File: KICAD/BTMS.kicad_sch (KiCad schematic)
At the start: 218 parts, among them J1 Batt_Ballance, J10 PWR_SW, J2 USB_C_Receptacle_4085, J3 AUX_Charge, J4 Battery_IO, J5 Power_Out, J6 DSKY, J7 BatteryPTC, J8 Heater, J9 ICSP, Q1 DMN65D8L, Q2 SSM3K341R, Q3 BSS84-7-F, Q5 DMN65D8L, Q6 SSM3K341R, Q7 BSS84-7-F, SW1 PTS526, U1 FAN3100TSX, U10 ACS711xLCTR-25AB, U11 ISL95808HRZ, U12 AON7522E, U13 AON7522E, U14 FAN3100TSX, U15 AON7522E, U16 LM62CIM3/NOPB, U17 FAN3100TSX, U18 AP62250Z6, U19 AP62250Z6, U2 DMP2240UDM, U20 dsPIC30F4011-PT, U21 FT230XQ, U22 MIC5504-3.3YM5, U23 DMP2240UDM, U24 DMP2240UDM, U25 DMP2240UDM, U26 DMP2240UDM, U3 Q294700DSGR, U4 ACS711xLCTR-25AB, U5 IS281-4, U6 SCF4030-12-0X, U7 AP33772, U8 IS281-4, U9 AONR21321

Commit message: Updated schematic and board to reflect changes made on prototype.
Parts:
- removed D10, D11: D_Schottky40V, Diode_SMD:D_0603_1608Metric, symbol Device:D
- removed R19: 0R, Resistor_SMD:R_1206_3216Metric, symbol Device:R
- added C64, C65: 10uf 25v BF, Capacitor_SMD:C_0805_2012Metric, symbol Device:C
- JP1: value SolderJumper_2_Open -> SolderJumper
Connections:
- net GND: now also C64.2, C65.2
- net VBUS: now also R17.1, U7.24 (VCC), C64.1, C65.1
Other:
- note added: "Battery Current and Output Control"
- note added: "Boost Drive"
- note added: "Buck Drive"
- note added: "Buck-Boost converter system"
- note added: "Cell Ballancing Control"
- note added: "Cell Voltage Analog Input Control"
- note added: "Charge Input Handling."
- note added: "Hardware Over Volt Protection"
- note added: "Heater Control"
- note added: "Power Enable Handling"
- note added: "USB serial"
- note added: "dsPIC and analog filtering."
- note removed: "Remove this 0 ohm resistor if USB charging is not desired."
- moved on the sheet: C1, C11, C12, C14, C15, C17, C19, C2, C21, C23, C25, C27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

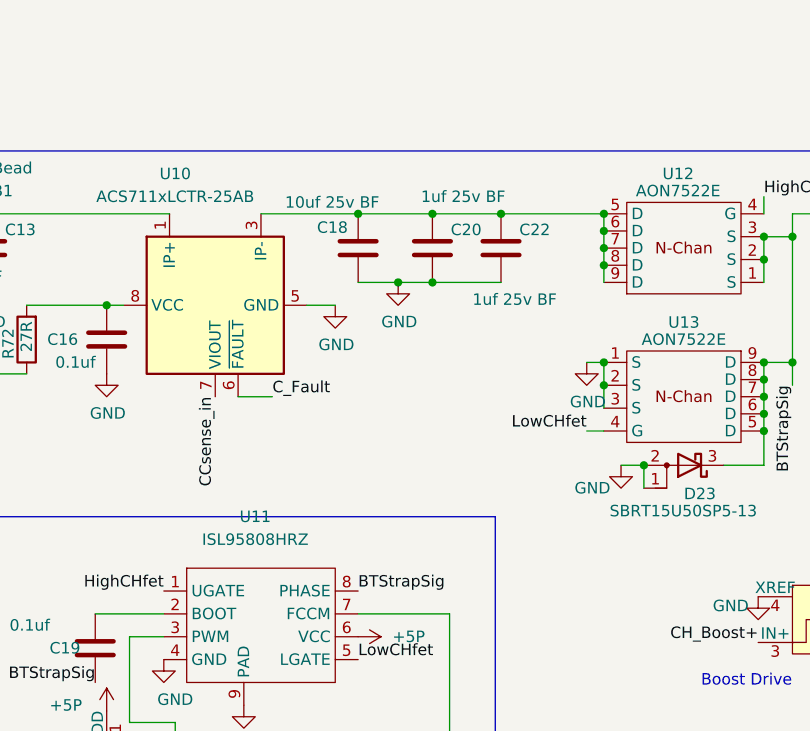
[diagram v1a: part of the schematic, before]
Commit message: Cleaned up some things in schematic and board. Deleted files not needed that were added to repo by mistake. Added 30uF of capacitors to input side of buck-boost converter.
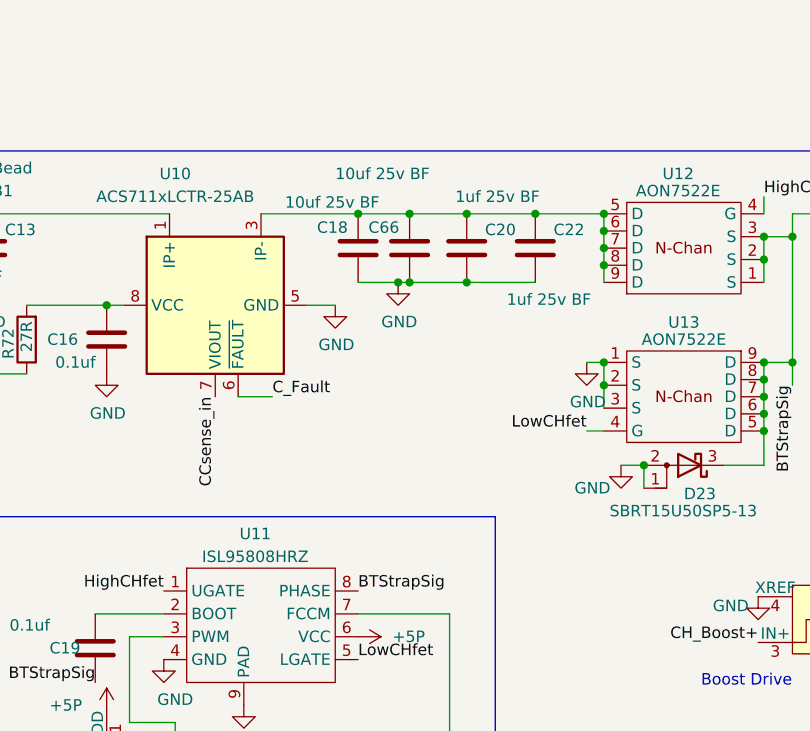
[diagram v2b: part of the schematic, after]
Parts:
- added C66: 10uf 25v BF, Capacitor_SMD:C_0805_2012Metric, symbol Device:C
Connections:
- net GND: now also C66.2
- net at C18.1, C20.1, C22.1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: now also C66.1
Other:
- moved on the sheet: C20, C22
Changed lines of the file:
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@@
   (junction (at 128.27 151.13) (diameter 0) (color 0 0 0 0)
   )
-  (junction (at 267.335 41.91) (diameter 0) (color 0 0 0 0)
+  (junction (at 264.795 41.91) (diameter 0) (color 0 0 0 0)
   )
   (junction (at 322.58 73.66) (diameter 0) (color 0 0 0 0)
@@
   (junction (at 126.365 292.1) (diameter 0) (color 0 0 0 0)
   )
+  (junction (at 278.765 41.91) (diameter 0) (color 0 0 0 0)
+  )
   (junction (at 219.075 395.605) (diameter 0) (color 0 0 0 0)
   )
@@
   (junction (at 348.615 51.435) (diameter 0) (color 0 0 0 0)
   )
-  (junction (at 274.955 41.91) (diameter 0) (color 0 0 0 0)
-  )
   (junction (at 538.48 151.13) (diameter 0) (color 0 0 0 0)
   )
@@
   (junction (at 424.18 81.915) (diameter 0) (color 0 0 0 0)
   )
+  (junction (at 271.145 41.91) (diameter 0) (color 0 0 0 0)
+  )
   (junction (at 523.24 46.99) (diameter 0) (color 0 0 0 0)
   )
@@
   (junction (at 537.845 327.025) (diameter 0) (color 0 0 0 0)
   )
+  (junction (at 264.795 49.53) (diameter 0) (color 0 0 0 0)
+  )
   (junction (at 535.305 327.025) (diameter 0) (color 0 0 0 0)
   )
@@
   (junction (at 245.745 276.86) (diameter 0) (color 0 0 0 0)
   )
-  (junction (at 267.335 49.53) (diameter 0) (color 0 0 0 0)
-  )
   (junction (at 245.745 269.24) (diameter 0) (color 0 0 0 0)
   )
@@
   (junction (at 464.82 260.985) (diameter 0) (color 0 0 0 0)
   )
+  (junction (at 271.145 49.53) (diameter 0) (color 0 0 0 0)
+  )
   (no_connect (at 47.5742 102.8192))
   (no_connect (at 47.5742 100.2792))
@@
     (stroke (width 0) (type default) (color 0 0 0 0))
   )
-  (wire (pts (xy 263.525 49.53) (xy 267.335 49.53))
+  (wire (pts (xy 263.525 49.53) (xy 264.795 49.53))
     (stroke (width 0) (type default) (color 0 0 0 0))
   )
@@
     (stroke (width 0) (type default) (color 0 0 0 0))
   )
-  (wire (pts (xy 267.335 49.53) (xy 274.955 49.53))
-    (stroke (width 0) (type default) (color 0 0 0 0))
-  )
   (wire (pts (xy 549.91 108.585) (xy 545.465 108.585))
     (stroke (width 0) (type default) (color 0 0 0 0))
@@
     (stroke (width 0) (type default) (color 0 0 0 0))
   )
-  (wire (pts (xy 259.08 41.91) (xy 267.335 41.91))
+  (wire (pts (xy 259.08 41.91) (xy 264.795 41.91))
     (stroke (width 0) (type default) (color 0 0 0 0))
   )
@@
     (stroke (width 0) (type default) (color 0 0 0 0))
   )
+  (wire (pts (xy 264.795 49.53) (xy 271.145 49.53))
+    (stroke (width 0) (type default) (color 0 0 0 0))
+  )
   (wire (pts (xy 117.475 43.815) (xy 121.92 43.815))
     (stroke (width 0) (type default) (color 0 0 0 0))
@@
     (stroke (width 0) (type default) (color 0 0 0 0))
   )
+  (wire (pts (xy 264.795 41.91) (xy 271.145 41.91))
+    (stroke (width 0) (type default) (color 0 0 0 0))
+  )
   (wire (pts (xy 481.33 339.09) (xy 487.68 339.09))
     (stroke (width 0) (type default) (color 0 0 0 0))
@@
     (stroke (width 0) (type default) (color 0 0 0 0))
   )
+  (wire (pts (xy 278.765 41.91) (xy 286.385 41.91))
+    (stroke (width 0) (type default) (color 0 0 0 0))
+  )
   (wire (pts (xy 514.985 82.55) (xy 514.985 83.82))
     (stroke (width 0) (type default) (color 0 0 0 0))
@@
     (stroke (width 0) (type default) (color 0 0 0 0))
   )
+  (wire (pts (xy 271.145 49.53) (xy 278.765 49.53))
+    (stroke (width 0) (type default) (color 0 0 0 0))
+  )
   (wire (pts (xy 522.605 93.98) (xy 528.955 93.98))
     (stroke (width 0) (type default) (color 0 0 0 0))
@@
     (stroke (width 0) (type default) (color 0 0 0 0))
   )
-  (wire (pts (xy 267.335 41.91) (xy 274.955 41.91))
-    (stroke (width 0) (type default) (color 0 0 0 0))
-  )
   (wire (pts (xy 187.325 356.235) (xy 187.325 363.855))
     (stroke (width 0) (type default) (color 0 0 0 0))
@@
     (stroke (width 0) (type default) (color 0 0 0 0))
   )
-  (wire (pts (xy 274.955 41.91) (xy 286.385 41.91))
+  (wire (pts (xy 271.145 41.91) (xy 278.765 41.91))
     (stroke (width 0) (type default) (color 0 0 0 0))
   )
@@
     (pin "2")
   )
-  (symbol (lib_id "Device:C") (at 267.335 45.72 0) (unit 1)
+  (symbol (lib_id "Device:C") (at 271.145 45.72 0) (unit 1)
     (in_bom yes) (on_board yes)
-    (property "Reference" "C20" (id 0) (at 269.367 43.688 0)
+    (property "Reference" "C20" (id 0) (at 273.177 43.688 0)
       (effects (font (size 1.27 1.27)) (justify left))
     )
-    (property "Value" "1uf 25v BF" (id 1) (at 266.065 40.005 0)
+    (property "Value" "1uf 25v BF" (id 1) (at 269.875 40.005 0)
       (effects (font (size 1.27 1.27)) (justify left))
     )
-    (property "Footprint" "Capacitor_SMD:C_0402_1005Metric" (id 2) (at 268.3002 49.53 0)
+    (property "Footprint" "Capacitor_SMD:C_0402_1005Metric" (id 2) (at 272.1102 49.53 0)
       (effects (font (size 1.27 1.27)) hide)
     )
-    (property "Datasheet" "~" (id 3) (at 267.335 45.72 0)
+    (property "Datasheet" "~" (id 3) (at 271.145 45.72 0)
       (effects (font (size 1.27 1.27)) hide)
     )
-    (property "DK_Detail_Page" "https://www.digikey.com/en/products/detail/tdk-corporation/C1005X5R1E105K050BE/7907739" (id 4) (at 267.335 45.72 0)
+    (property "DK_Detail_Page" "https://www.digikey.com/en/products/detail/tdk-corporation/C1005X5R1E105K050BE/7907739" (id 4) (at 271.145 45.72 0)
       (effects (font (size 1.27 1.27)) hide)
     )
-    (property "Digi-Key_PN" "445-175215-1-ND" (id 5) (at 267.335 45.72 0)
+    (property "Digi-Key_PN" "445-175215-1-ND" (id 5) (at 271.145 45.72 0)
       (effects (font (size 1.27 1.27)) hide)
     )
@@
   )
   (symbol (lib_name "ISL95808HRZ_1") (lib_id "New_Library:ISL95808HRZ") (at 247.65 87.63 0) (unit 1)
-    (in_bom yes) (on_board yes) (fields_autoplaced)
-    (property "Reference" "U11" (id 0) (at 247.65 75.565 0))
-    (property "Value" "ISL95808HRZ" (id 1) (at 247.65 78.105 0))
+    (in_bom yes) (on_board yes)
+    (property "Reference" "U11" (id 0) (at 247.65 77.47 0))
+    (property "Value" "ISL95808HRZ" (id 1) (at 247.65 80.01 0))
     (property "Footprint" "Package_DFN_QFN:DFN-8-1EP_2x2mm_P0.5mm_EP0.8x1.6mm" (id 2) (at 247.65 70.485 0)
       (effects (font (size 1.27 1.27)) hide)
@@
     (pin "2")
   )
+  (symbol (lib_id "Device:C") (at 264.795 45.72 0) (unit 1)
+    (in_bom yes) (on_board yes)
+    (property "Reference" "C66" (id 0) (at 260.223 43.434 0)
+      (effects (font (size 1.27 1.27)) (justify left))
+    )
+    (property "Value" "10uf 25v BF" (id 1) (at 256.54 37.465 0)
+      (effects (font (size 1.27 1.27)) (justify left))
+    )
+    (property "Footprint" "Capacitor_SMD:C_0805_2012Metric" (id 2) (at 265.7602 49.53 0)
+      (effects (font (size 1.27 1.27)) hide)
+    )
+    (property "Datasheet" "~" (id 3) (at 264.795 45.72 0)
+      (effects (font (size 1.27 1.27)) hide)
+    )
+    (property "DK_Detail_Page" "https://www.digikey.com/en/products/detail/murata-electronics/GRJ21BR61E106KE01K/10705983" (id 4) (at 264.795 45.72 0)
+      (effects (font (size 1.27 1.27)) hide)
+    )
+    (property "Digi-Key_PN" "490-GRJ21BR61E106KE01KCT-ND" (id 5) (at 264.795 45.72 0)
+      (effects (font (size 1.27 1.27)) hide)
+    )
+    (pin "1")
+    (pin "2")
+  )
   (symbol (lib_id "Device:C") (at 407.67 341.63 0) (unit 1)
     (in_bom yes) (on_board yes)
@@
     (pin "1")
   )
-  (symbol (lib_id "Device:C") (at 274.955 45.72 0) (unit 1)
+  (symbol (lib_id "Device:C") (at 278.765 45.72 0) (unit 1)
     (in_bom yes) (on_board yes)
-    (property "Reference" "C22" (id 0) (at 276.987 43.688 0)
+    (property "Reference" "C22" (id 0) (at 280.797 43.688 0)
       (effects (font (size 1.27 1.27)) (justify left))
     )
-    (property "Value" "1uf 25v BF" (id 1) (at 271.78 51.435 0)
+    (property "Value" "1uf 25v BF" (id 1) (at 275.59 51.435 0)
       (effects (font (size 1.27 1.27)) (justify left))
     )
-    (property "Footprint" "Capacitor_SMD:C_0402_1005Metric" (id 2) (at 275.9202 49.53 0)
+    (property "Footprint" "Capacitor_SMD:C_0402_1005Metric" (id 2) (at 279.7302 49.53 0)
       (effects (font (size 1.27 1.27)) hide)
     )
-    (property "Datasheet" "~" (id 3) (at 274.955 45.72 0)
+    (property "Datasheet" "~" (id 3) (at 278.765 45.72 0)
       (effects (font (size 1.27 1.27)) hide)
     )
-    (property "DK_Detail_Page" "https://www.digikey.com/en/products/detail/tdk-corporation/C1005X5R1E105K050BE/7907739" (id 4) (at 274.955 45.72 0)
+    (property "DK_Detail_Page" "https://www.digikey.com/en/products/detail/tdk-corporation/C1005X5R1E105K050BE/7907739" (id 4) (at 278.765 45.72 0)
       (effects (font (size 1.27 1.27)) hide)
     )
-    (property "Digi-Key_PN" "445-175215-1-ND" (id 5) (at 274.955 45.72 0)
+    (property "Digi-Key_PN" "445-175215-1-ND" (id 5) (at 278.765 45.72 0)
       (effects (font (size 1.27 1.27)) hide)
     )
@@
       (reference "C65") (unit 1) (value "10uf 25v BF") (footprint "Capacitor_SMD:C_0805_2012Metric")
     )
+    (path "/8720c524-b4ed-489c-9123-369ca428054a"
+      (reference "C66") (unit 1) (value "10uf 25v BF") (footprint "Capacitor_SMD:C_0805_2012Metric")
+    )
     (path "/6ca46fb0-edf1-4589-8ace-172ff9647bed"

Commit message: Updated REV1B(P)_schematic. Made copy of REV1A(P) schematic and board layout. Found a few diodes to be leaking current when in sleep mode. Need to fix.
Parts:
- removed D26, D27, D28: D_Schottky40V, Diode_SMD:D_0603_1608Metric, symbol Device:D
- removed Q7: BSS84-7-F, Package_TO_SOT_SMD:SOT-23, symbol Device:Q_PMOS_GSD
- removed R52: 1K, Resistor_SMD:R_0603_1608Metric, symbol Device:R
- removed RN12: 10K, Resistor_SMD:R_Array_Convex_4x0612, symbol Device:R_Pack04
- added C? (x2): 10uf 25v BF, Capacitor_SMD:C_0805_2012Metric, symbol Device:C
- added Q? (x2): DMN65D8L, Package_TO_SOT_SMD:SOT-23, symbol Device:Q_NMOS_GSD
- added R? (x6): 10K, Resistor_SMD:R_0603_1608Metric, symbol Device:R
- added R? (x2): 1M, Resistor_SMD:R_0603_1608Metric, symbol Device:R
- added R?: 1K, Resistor_SMD:R_0603_1608Metric, symbol Device:R
- added R?: 27R, Resistor_SMD:R_0603_1608Metric, symbol Device:R
- added U?: DMP2240UDM, Package_TO_SOT_SMD:SOT-23-6, symbol New_Library:DMP2240UDM
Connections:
- net SW_Signal is gone; now on an unnamed net: RN9.1 (R1.1)
- net +3.3VP: now also Q?.1 (G), R?.2
- net GND: now also RN9.8 (R1.2), Q?.2 (S), Q?.2 (S), R?.1, R?.1, R?.1
- net IntBus: now also R?.2, R?.2, U?.2 (S2), U?.5 (S1); no longer C32.1, L2.1
- net KeepAlive: now also R?.1
- net Pwr_Sw: now reaches C56.1, D6.1 (K), J10.1, SW1.2 (B)
- net Pwr_Sw: now also C?.2, R?.1
- net at D33.2 (A): now also C?.1, R?.1, R?.2, U?.3 (G2)
- net at C37.1, C38.1, L2.2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: now also R?.2
- net at R42.1, U18.6 (FB): now also R?.2
- net Power_EN: no longer names the net of D29.1 (K), U18.5 (EN), U19.5 (EN)
- net Power_EN: now also R?.1
- new net: C?.2, Q?.3 (D), R?.1
- new net: C?.1, Q?.3 (D), R?.1, R?.2, U?.1 (G1)
- new net: C32.1, L2.1, R?.2
- new net: Q?.1 (G), R?.2, R?.2
- new net: R?.1, U?.4 (D2), U?.6 (D1)
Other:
- moved on the sheet: C13, C16, C18, C19, C20, C21, C22, C24, C25, C27, C28, C32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

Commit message: Added I2C ADC to REV.1B board. Added Battery Disconnect system to REV.1B board. Changed some dsPIC IO around to reflect changes. Changed power control system to not drain battery very quickly if switch or charger input is held in the 'on' state. We will see how this works. Started placing and re-routing board to reflect schematic.
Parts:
- removed D23, D24: SBRT15U50SP5-13, Package_TO_SOT_SMD:TO-277B, symbol Device:D_Schottky_AAK
- removed R15, R16: 12, Resistor_SMD:R_0603_1608Metric, symbol Device:R
- removed R62, R72: 27R, Resistor_SMD:R_0603_1608Metric, symbol Device:R
- removed U14: FAN3100TSX, Package_TO_SOT_SMD:SOT-23-5, symbol BTMS-rescue:FAN3111ESX-dk_PMIC-Gate-Drivers
- added C69, C71: 1uf 25v BF, Capacitor_SMD:C_0402_1005Metric, symbol Device:C
- added C70: 0.1uf, Capacitor_SMD:C_0402_1005Metric, symbol Device:C
- added D11: BAV23CLT1G, Package_TO_SOT_SMD:SOT-23, symbol Diode:BAV70
- added Q4: DMN65D8L, Package_TO_SOT_SMD:SOT-23, symbol Device:Q_NMOS_GSD
- added R19, R20, R25: 1K, Resistor_SMD:R_0603_1608Metric, symbol Device:R
- added R27: 10K*, Resistor_SMD:R_0603_1608Metric, symbol Device:R
- added R30: 1K*, Resistor_SMD:R_0603_1608Metric, symbol Device:R
- added U14, U27: AONR21321, Package_DFN_QFN:DFN-8-1EP_3x3mm_P0.65mm_EP1.7x2.05mm, symbol New_Library:AONR21321
- added U28: FAN3100TSX, Package_TO_SOT_SMD:SOT-23-5, symbol BTMS-rescue:FAN3111ESX-dk_PMIC-Gate-Drivers
- added U29: ISL95808HRZ, Package_DFN_QFN:DFN-8-1EP_2x2mm_P0.5mm_EP0.8x1.6mm, symbol New_Library:ISL95808HRZ
- added U30: AON7522E, Package_DFN_QFN:DFN-8-1EP_3x3mm_P0.65mm_EP1.7x2.05mm, symbol New_Library:AON7522E
- added U32: MCP3021, Package_TO_SOT_SMD:SOT-23-5, symbol adc:MCP3021
- C30: value 1uf 25v BF -> 0.1uf; DK_Detail_Page https://www.digikey.com/en/products/detail/tdk-corporation/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 -> https://www.digikey.com/en/products/detail/samsung-electro-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; Digi-Key_PN 445-175215-1-ND -> 1276-1043-1-ND
- gave numbers to parts that had none: 15
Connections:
- net +3.3VA: now also C16.1, C7.1, U10.8 (VCC), U4.8 (VCC)
- net +3V3: now also C70.1, U32.1 (Vdd)
- net +5P: now also U28.1 (VDD), U29.6 (VCC), U29.7 (FCCM)
- net BTStrapSig: now also C30.2, U29.8 (PHASE)
- net CH_Boost+: now also R25.1
- net ExtBus: now also D11.2 (A), R27.2, U27.1 (S), U27.2 (S), U27.3 (S); no longer U6.3 (T2)
- net GND: now also C69.2, C70.2, C71.2, Q4.2 (S), R20.2, R30.2, U28.2 (GND), U28.4 (XREF), U29.4 (GND), U29.9 (PAD), U32.2 (Vss); no longer C30.2
- net IntBus: now also U6.3 (T2), D11.1 (A); no longer D33.1 (K), R43.2, R49.2, U31.2 (S2), U31.5 (S1), U6.1 (T1)
- net PGMC: now also U7.4 (SDA), U32.4 (SDA)
- net PGMD: now also U7.5 (SCL), U32.5 (SCL)
- net PowerOutEnable: now also R6.2
- net at U16.2 (D): now also C69.1, U32.3 (Ain); no longer RN8.4 (R4.1)
- net at L1.2, U15.5 (D), U15.6 (D)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: now also U30.1 (S), U30.2 (S), U30.3 (S)
- net at C25.1, C27.1, C58.1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: now also U30.5 (D), U30.6 (D), U30.7 (D), U30.8 (D), U30.9 (D)
- net LowBTfet: now reaches U15.4 (G)
- net LowBTfet: now also U29.5 (LGATE)
- net Pre-Charge renamed BattConnect
- net BattConnect: now also Q4.1 (G), R20.1; no longer R6.2
- new net: R25.2, U28.3 (IN+)
- new net: C30.1, U29.2 (BOOT)
- new net: U28.5 (OUT), U29.3 (PWM)
- new net: Q4.3 (D), R19.1, U14.4 (G), U27.4 (G)
- new net: U14.5 (D), U14.6 (D), U14.7 (D), U14.8 (D), U14.9 (D), U27.5 (D), U27.6 (D), U27.7 (D), U27.8 (D), U27.9 (D)
- new net Ext_Bus_Vsense: C71.1, R27.1, R30.1, U20.22 (AN3/INDX/CN5/RB3)
- new net HighBTfet: U29.1 (UGATE), U30.4 (G)
- new net MidBus: R19.2, U14.1 (S), U14.2 (S), U14.3 (S), U6.1 (T1)
- new net SysBus: D11.3 (K), D33.1 (K), R43.2, R49.2, U31.2 (S2), U31.5 (S1)
- now unconnected: RN8.5 (R4.2)
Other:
- note added: "Board Temperature Sensor"
- moved on the sheet: C12, C14, C15, C17, C19, C21, C23, C25, C26, C27, C28, C29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

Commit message: Updated board layout for REV. B Completed initial routing. Need to finish fixing circuit changes such as inrush current limiting. Need to refine board layout.
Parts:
- removed C67: 10uf 25v BF, Capacitor_SMD:C_0805_2012Metric, symbol Device:C
- removed D7: D_Schottky40V, Diode_SMD:D_0603_1608Metric, symbol Device:D
- removed Q1: DMN65D8L, Package_TO_SOT_SMD:SOT-23, symbol Device:Q_NMOS_GSD
- removed R10, R29, R7: 10K, Resistor_SMD:R_0603_1608Metric, symbol Device:R
- removed R32: 1M, Resistor_SMD:R_0603_1608Metric, symbol Device:R
- removed R6: 1K, Resistor_SMD:R_0603_1608Metric, symbol Device:R
- removed R8, R9: 150, Resistor_SMD:R_0805_2012Metric_Pad1.20x1.40mm_HandSolder, symbol Device:R
- removed U2: DMP2240UDM, Package_TO_SOT_SMD:SOT-23-6, symbol New_Library:DMP2240UDM
- added R15: 1K, Resistor_SMD:R_0603_1608Metric, symbol Device:R
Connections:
- net +3.3VP: now also R15.1
- net BTStrapSig: no longer C30.2, U29.8 (PHASE)
- net ExtBus: now also U14.5 (D), U14.6 (D), U14.7 (D), U14.8 (D), U14.9 (D); no longer U27.1 (S), U27.2 (S), U27.3 (S)
- net GND: now also R15.2
- net MidBus: now also U27.5 (D), U27.6 (D), U27.7 (D), U27.8 (D), U27.9 (D); no longer R19.2, U14.1 (S), U14.2 (S), U14.3 (S)
- net BoostBTStrapSig: now reaches L1.2, U15.5 (D), U15.6 (D), U15.7 (D), U15.8 (D), U15.9 (D), U30.1 (S), U30.2 (S), U30.3 (S)
- net BoostBTStrapSig: now also C30.2, U29.8 (PHASE)
- net at Q7.3 (D): now also Q8.3 (D), R43.1, U31.1 (G1)
- net ExtBus_RES: no longer names the net of Q5.3 (D), RN11.5 (R4.2), U9.4 (G)
- new net: R19.2, U14.1 (S), U14.2 (S), U14.3 (S), U27.1 (S), U27.2 (S), U27.3 (S)
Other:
- moved on the sheet: J5, R19, U14, U27

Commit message: Worked on improving routing.
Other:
- note added: "Battery Current sensing and Output Control"
- note removed: "Battery Current and Output Control"
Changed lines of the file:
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@@
     (effects (font (size 1.27 1.27)) (justify left bottom))
   )
-  (text "Battery Current and Output Control" (at 146.685 220.98 0)
+  (text "Battery Current sensing and Output Control" (at 140.97 220.98 0)
     (effects (font (size 1.27 1.27)) (justify left bottom))
   )
@@
   )
   (text "Using digital 3.3v instead of analog for\nthis temperature sensor because it's not\nsuper ciritial how accurate it is, and this\npower line runs accross the board and could\npickup noise."
-    (at 422.91 389.255 0)
+    (at 422.91 391.16 0)
     (effects (font (size 1.27 1.27)) (justify left bottom))
   )

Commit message: Finished implementing inrush current limiting changes. Need to verify design. Need to clean up tails and islands. Need to create BOM.
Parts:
- removed R19: 1K, Resistor_SMD:R_0603_1608Metric, symbol Device:R
- added C67, C72: 10uf 25v BF, Capacitor_SMD:C_0805_2012Metric, symbol Device:C
- added R6, R7, R9: 5K, Resistor_SMD:R_0603_1608Metric, symbol Device:R
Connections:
- net ExtBus: now also C72.1
- net at U14.1 (S), U14.2 (S), U14.3 (S)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: now also C67.2, R7.1
- net at U14.4 (G), U27.4 (G): now also C67.1, R6.1, R7.2; no longer Q4.3 (D)
- net at RN11.5 (R4.2), U9.4 (G): now also C72.2, R9.2; no longer Q5.3 (D)
- new net: Q4.3 (D), R6.2
- new net: Q5.3 (D), R9.1
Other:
- moved on the sheet: C11, J5, Q4, R20, U9
